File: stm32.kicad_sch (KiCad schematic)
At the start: 5 parts, among them U2 STM32C542CCT6, U3 STM32G431RBT6

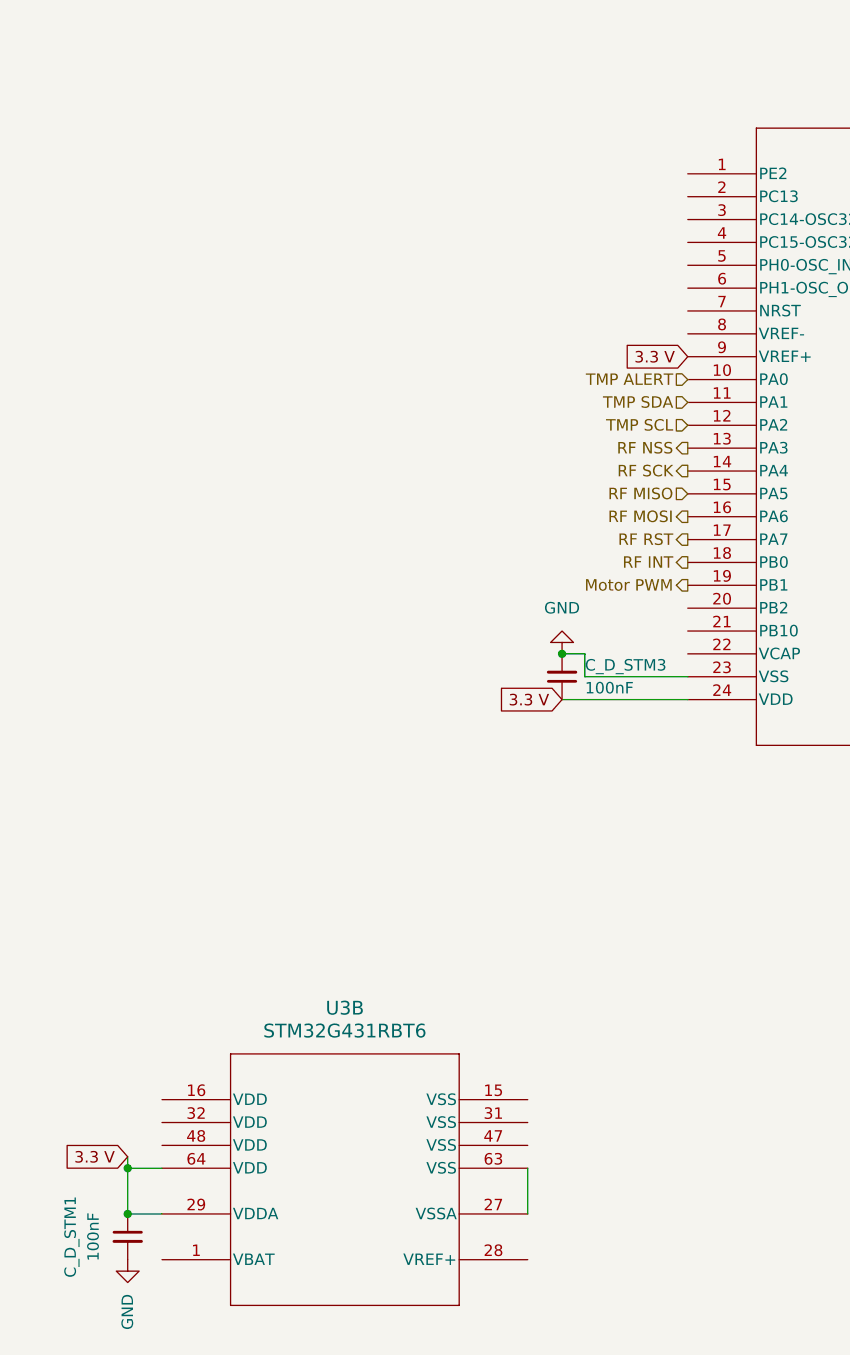
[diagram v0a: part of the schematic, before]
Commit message: todolist update
update of the to do list on schematic
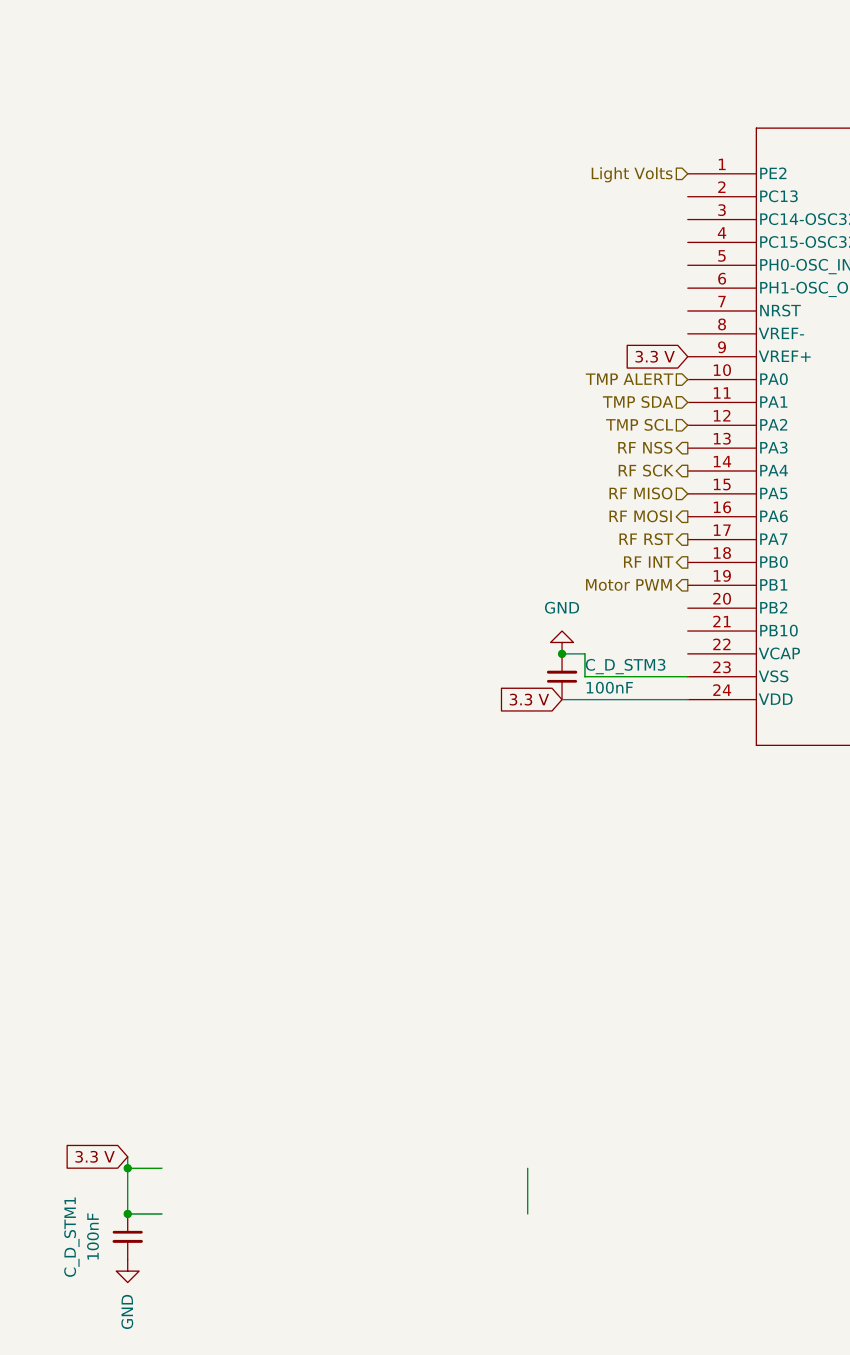
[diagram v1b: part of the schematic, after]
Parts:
- removed U2: STM32C542CCT6, LQFP48-7X7, symbol STM32:STM32C542CCT6
- removed U3: STM32G431RBT6, stm32:LQFP64-10x10mm, symbol stm32:STM32G431RBT6
- added U2: STM32C542CCT6, rov_logic:LQFP48-7X7, symbol rov_logic:STM32C542CCT6
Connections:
- net 3.3 V: now also U2.24 (VDD), U2.48 (VDD), U2.9 (VREF+)
- net Depth SCL: now also U2.39 (PB3)
- net Depth SDA: now also U2.40 (PB4)
- net GND: now also U2.23 (VSS), U2.47 (VSS)
- net INA ALERT: now also U2.41 (PB5)
- net INA SCL: now also U2.42 (PB6)
- net INA SDA: now also U2.43 (PB7)
- net Motor PWM: now also U2.19 (PB1)
- net RF INT: now also U2.18 (PB0)
- net RF MISO: now also U2.15 (PA5)
- net RF MOSI: now also U2.16 (PA6)
- net RF NSS: now also U2.13 (PA3)
- net RF RST: now also U2.17 (PA7)
- net RF SCK: now also U2.14 (PA4)
- net Switch: now also U2.38 (PA15)
- net TMP ALERT: now also U2.10 (PA0)
- net TMP SCL: now also U2.12 (PA2)
- net TMP SDA: now also U2.11 (PA1)
- net USB BUS: now also U2.33 (PA12)
- net USB DN: now also U2.32 (PA11)
- net USB DP: now also U2.31 (PA10)
- new net Light Volts: U2.1 (PE2)

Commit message: Updated Schematic
Updated parts of todo list for schematic
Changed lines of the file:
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@@
-		)
-	)
-	(hierarchical_label "USB DP"
-		(shape input)
-		(at 358.14 1.27 0)
-		(effects
-			(font
-				(size 1.27 1.27)
-			)
-			(justify left)
 		)
 	)

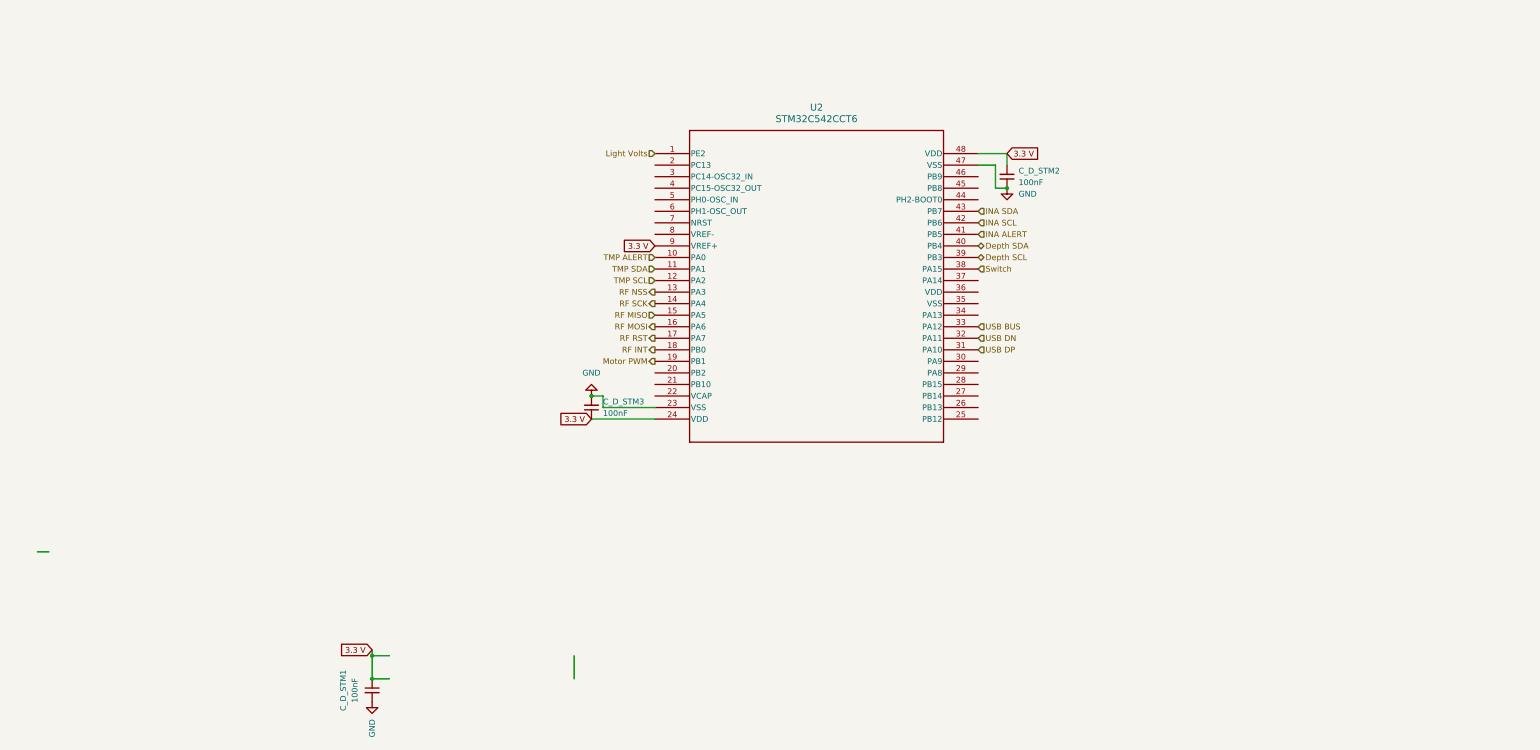
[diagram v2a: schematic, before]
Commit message: Updated Schematic
Updated schematic
Cleaned up dense portions
added H bridge
correct i2c wiring
added ferrite beads
added 12 V power monitoring
added stlink
added power mux
added power from usb
reformatted hierarichal sheets
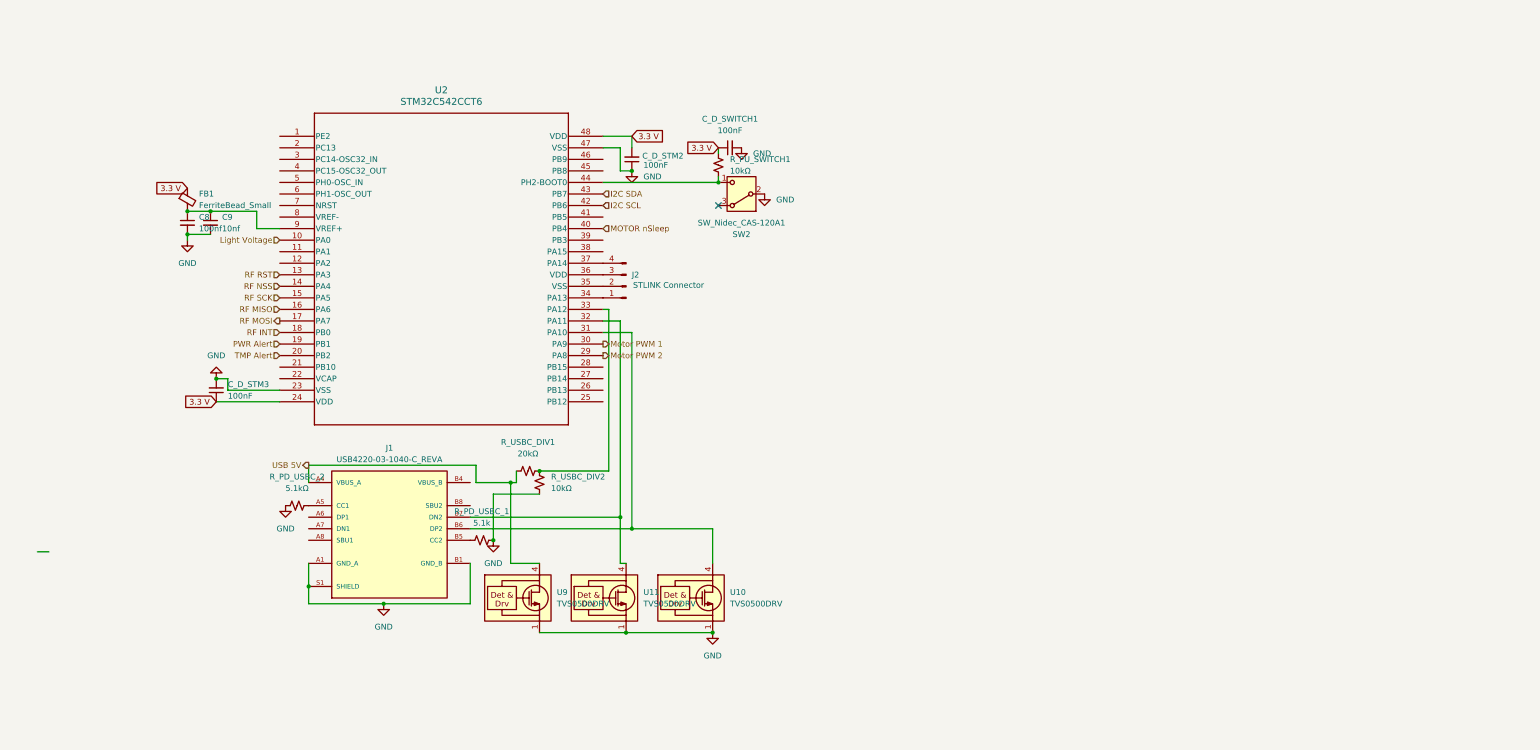
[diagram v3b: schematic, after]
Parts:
- removed C_D_STM1: 100nF, Capacitor_SMD:C_0603_1608Metric, symbol Device:C_Small
- added C8: 100nf, symbol Device:C_Small
- added C9: 10nf, symbol Device:C_Small
- added C_D_SWITCH1: 100nF, Capacitor_SMD:C_0603_1608Metric, symbol Device:C_Small
- added FB1: FerriteBead_Small, symbol Device:FerriteBead_Small
- added J1: USB4220-03-1040-C_REVA, usbc:GCT_USB4220-03-1040-C_REVA, symbol usbc:USB4220-03-1040-C_REVA
- added J2: STLINK Connector, symbol Connector:Conn_01x04_Pin
- added R_PD_USBC_1: 5.1k, Resistor_SMD:R_0603_1608Metric, symbol Device:R_Small_US
- added R_PD_USBC_2: 5.1kΩ, Resistor_SMD:R_0603_1608Metric, symbol Device:R_Small_US
- added R_PU_SWITCH1: 10kΩ, Resistor_SMD:R_0603_1608Metric, symbol Device:R_Small_US
- added R_USBC_DIV1: 20kΩ, Resistor_SMD:R_0603_1608Metric, symbol Device:R_Small_US
- added R_USBC_DIV2: 10kΩ, Resistor_SMD:R_0603_1608Metric, symbol Device:R_Small_US
- added SW2: SW_Nidec_CAS-120A1, Button_Switch_SMD:Nidec_Copal_CAS-120A, symbol Switch:SW_Nidec_CAS-120A1
- added U10, U11, U9: TVS0500DRV, Package_SON:WSON-6-1EP_2x2mm_P0.65mm_EP1x1.6mm, symbol Power_Protection:TVS0500DRV
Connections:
- net 3.3 V: now also C_D_SWITCH1.1, FB1.1, R_PU_SWITCH1.2; no longer U2.9 (VREF+)
- net GND: now also C8.2, C9.2, C_D_SWITCH1.2, J1.A1 (GND_A), J1.A12 (GND_A), J1.B1 (GND_B), J1.B12 (GND_A), J1.S1 (SHIELD), J1.S2 (SHIELD), J1.S3 (SHIELD), J1.S4 (SHIELD), R_PD_USBC_1.2, R_PD_USBC_2.1, R_USBC_DIV2.2, SW2.2 (B), U10.1 (GND), U10.2 (GND), U10.3 (GND), U10.7 (GND), U11.1 (GND), U11.2 (GND), U11.3 (GND), U11.7 (GND), U9.1 (GND), U9.2 (GND), U9.3 (GND), U9.7 (GND)
- net RF MISO: now also U2.16 (PA6); no longer U2.15 (PA5)
- net RF MOSI: now also U2.17 (PA7); no longer U2.16 (PA6)
- net RF NSS: now also U2.14 (PA4); no longer U2.13 (PA3)
- net RF RST: now also U2.13 (PA3); no longer U2.17 (PA7)
- net RF SCK: now also U2.15 (PA5); no longer U2.14 (PA4)
- net TMP Alert: now reaches U2.20 (PB2)
- net Motor PWM 2: now reaches U2.29 (PA8)
- net Motor PWM 1: now reaches U2.30 (PA9)
- net at U2.34 (PA13): now also J2.1 (Pin_1)
- net at U2.35 (VSS): now also J2.2 (Pin_2)
- net at U2.36 (VDD): now also J2.3 (Pin_3)
- net at U2.37 (PA14): now also J2.4 (Pin_4)
- net at U2.44 (PH2-BOOT0): now also R_PU_SWITCH1.1, SW2.1 (C)
- net Depth SCL: no longer names the net of U2.39 (PB3)
- net Depth SDA renamed MOTOR nSleep
- net INA ALERT: no longer names the net of U2.41 (PB5)
- net INA SCL renamed I2C SCL
- net INA SDA renamed I2C SDA
- net Light Volts: no longer names the net of U2.1 (PE2)
- net Motor PWM renamed PWR Alert
- net Switch: no longer names the net of U2.38 (PA15)
- net TMP ALERT renamed Light Voltage
- net TMP SCL: no longer names the net of U2.12 (PA2)
- net TMP SDA: no longer names the net of U2.11 (PA1)
- net USB BUS: no longer names the net of U2.33 (PA12)
- net USB BUS: now also R_USBC_DIV1.2, R_USBC_DIV2.1
- net USB DN: no longer names the net of U2.32 (PA11)
- net USB DN: now also J1.B7 (DN2), U11.4 (IN), U11.5 (IN), U11.6 (IN)
- net USB DP: no longer names the net of U2.31 (PA10)
- net USB DP: now also J1.B6 (DP2), U10.4 (IN), U10.5 (IN), U10.6 (IN)
- new net: J1.A5 (CC1), R_PD_USBC_2.2
- new net: C8.1, C9.1, FB1.2, U2.9 (VREF+)
- new net: J1.B5 (CC2), R_PD_USBC_1.1
- new net VBUS_A: J1.A4 (VBUS_A), J1.A9 (VBUS_A), R_USBC_DIV1.1, U9.4 (IN), U9.5 (IN), U9.6 (IN)
- new net VBUS_B: J1.B4 (VBUS_B), J1.B9 (VBUS_B)
- no-connect marks 0 -> 1
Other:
- moved on the sheet: C_D_STM2, C_D_STM3, U2

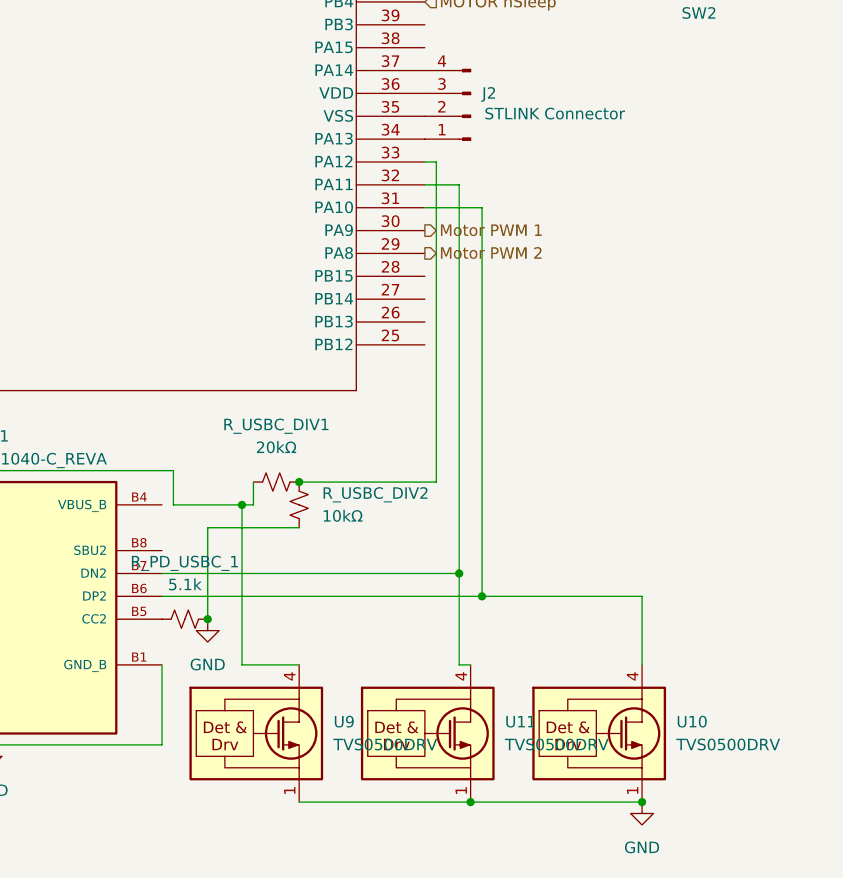
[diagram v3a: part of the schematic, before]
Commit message: USB, TVS, LDO, Passives, I2C
applied changes to usb circuitry, tvs, ldo, passibes and i2c.
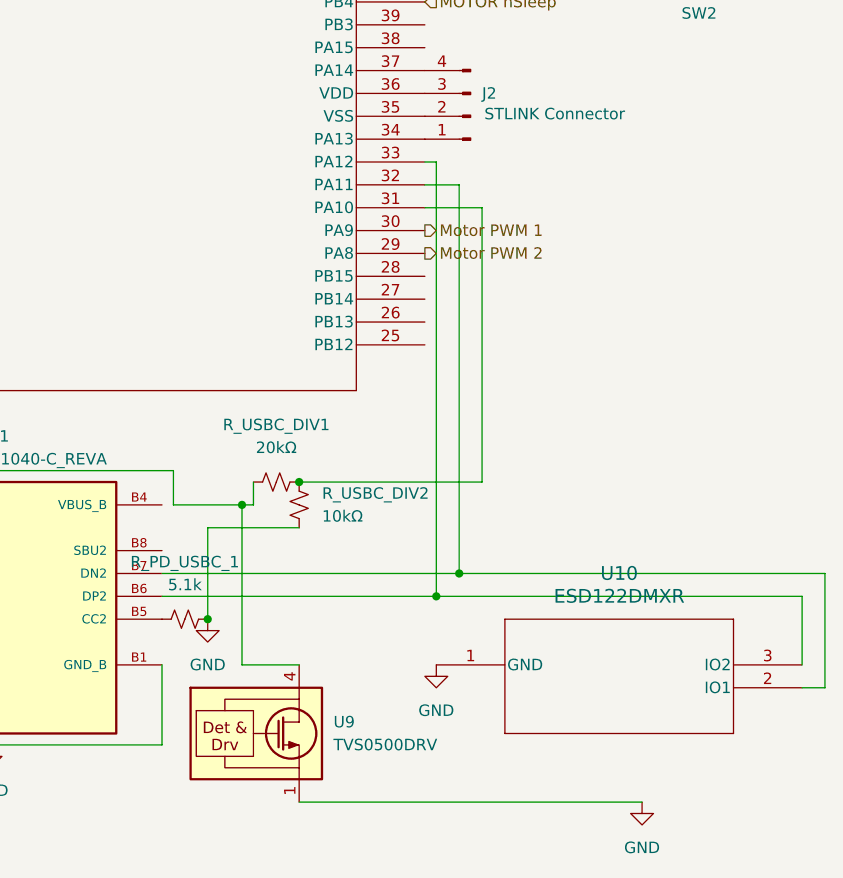
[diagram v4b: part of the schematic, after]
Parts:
- removed U10, U11: TVS0500DRV, Package_SON:WSON-6-1EP_2x2mm_P0.65mm_EP1x1.6mm, symbol Power_Protection:TVS0500DRV
- added U10: ESD122DMXR, DMX3_TEX, symbol TVSdiodeusb:ESD122DMXR
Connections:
- net GND: now also U10.1 (GND)
- net at R_USBC_DIV1.2, R_USBC_DIV2.1: now also U2.31 (PA10); no longer U2.33 (PA12)
- net at J1.B6 (DP2): now also U2.33 (PA12), U10.3 (IO2); no longer U2.31 (PA10)
- net at J1.B7 (DN2), U2.32 (PA11): now also U10.2 (IO1)

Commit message: float
float for claude review
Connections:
- net VBUS_B is gone; now on net VBUS_A: J1.B4 (VBUS_B), J1.B9 (VBUS_B)
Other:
- note added: "Add button for nrst, connect vref - check stlink gpio connect usb dn and dp so both orientations of usb work"
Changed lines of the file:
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@@
 	(generator_version "10.0")
 	(paper "A4")
+	(text "Add button for nrst, connect vref -\ncheck stlink gpio\nconnect usb dn and dp so both orientations of usb work\n\n"
+		(exclude_from_sim no)
+		(at 86.106 16.764 0)
+		(effects
+			(font
+				(size 1.27 1.27)
+			)
+		)
+	)
 	(junction
 		(at 72.39 49.53)
@@
 	(junction
 		(at 189.23 38.1)
+		(diameter 0)
+		(color 0 0 0 0)
+	)
+	(junction
+		(at 135.89 104.14)
 		(diameter 0)
 		(color 0 0 0 0)
@@
 		)
 		(stroke
+			(width 0)
+			(type default)
+		)
+	)
+	(wire
+		(pts
+			(xy 134.62 104.14) (xy 135.89 104.14)
+		)
+		(stroke

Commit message: footprints
footprints
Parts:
- removed C9: 10nf, symbol Device:C_Small
- removed FB1: FerriteBead_Small, symbol Device:FerriteBead_Small
- removed SW2: SW_Nidec_CAS-120A1, Button_Switch_SMD:Nidec_Copal_CAS-120A, symbol Switch:SW_Nidec_CAS-120A1
- removed U9: TVS0500DRV, Package_SON:WSON-6-1EP_2x2mm_P0.65mm_EP1x1.6mm, symbol Power_Protection:TVS0500DRV
- added C_D_STM4: 2.2uF, Capacitor_SMD:C_0603_1608Metric, symbol Device:C_Small
- added C_D_SWITCH2: 100nF, Capacitor_SMD:C_0603_1608Metric, symbol Device:C_Small
- added R_PU_SWITCH2: 10kΩ, Resistor_SMD:R_0603_1608Metric, symbol Device:R_Small_US
- added SW1, SW2: EG1218, CustomFootprints:EG_1218_EWI, symbol switch:EG1218
- added U8: TPD1E05U06DPY, Package_SON:Texas_DPY0002A_0.6x1mm_P0.65mm, symbol Power_Protection:TPD1E05U06DPY
- C8: footprint (none) -> Capacitor_SMD:C_0603_1608Metric_Pad1.08x0.95mm_HandSolder
- J1: footprint usbc:GCT_USB4220-03-1040-C_REVA -> CustomFootprints:GCT_USB4220-03-1040-C_REVA
- U10: footprint DMX3_TEX -> CustomFootprints:DMX3_TEX
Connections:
- net 3.3 V: now also C8.1, C_D_STM3.2, C_D_SWITCH1.2, U2.9 (VREF+), C_D_SWITCH2.1, R_PU_SWITCH2.1, SW2.1; no longer C_D_STM3.1, C_D_SWITCH1.1, R_PU_SWITCH1.2
- net GND: now also C_D_STM3.1, C_D_SWITCH1.1, R_PU_SWITCH1.1, R_USBC_DIV1.1, U2.8 (VREF-), C_D_STM4.1, C_D_SWITCH2.2, SW1.1, U8.1 (I/O); no longer C_D_STM3.2, C_D_SWITCH1.2, R_USBC_DIV2.2
- net VBUS_A: now also R_USBC_DIV2.1, U8.2 (GND); no longer R_USBC_DIV1.1
- net at R_USBC_DIV1.2, U2.31 (PA10): now also R_USBC_DIV2.2; no longer R_USBC_DIV2.1
- net at U2.44 (PH2-BOOT0): now also R_PU_SWITCH1.2, SW2.3; no longer R_PU_SWITCH1.1
- net at U2.22 (VCAP): now also C_D_STM4.2
- net at J1.B7 (DN2), U10.2 (IO1), U2.32 (PA11): now also J1.A7 (DN1)
- net at J1.B6 (DP2), U10.3 (IO2), U2.33 (PA12): now also J1.A6 (DP1)
- net at U2.7 (NRST): now also R_PU_SWITCH2.2, SW1.3
- no-connect marks 1 -> 2
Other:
- note removed: "Add button for nrst, connect vref - check stlink gpio connect usb dn and dp so both orientations of usb work"
- moved on the sheet: C8, C_D_SWITCH1

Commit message: Finished footprints
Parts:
- J2: footprint (none) -> Connector_PinHeader_1.27mm:PinHeader_2x05_P1.27mm_Vertical_SMD
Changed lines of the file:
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@@
 			)
 		)
-		(property "Footprint" ""
+		(property "Footprint" "Connector_PinHeader_1.27mm:PinHeader_2x05_P1.27mm_Vertical_SMD"
 			(at 168.91 60.96 0)
 			(hide yes)
